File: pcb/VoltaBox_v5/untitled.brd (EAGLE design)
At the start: 80 x 60 mm, 63 parts, among them J1 0, X1 112J-TDAR-R(MICROSD), X2 52892-0895, X3 52892-0895, X4 XT30PW-F, X6 XT60PW-M, X7 KLS1-233

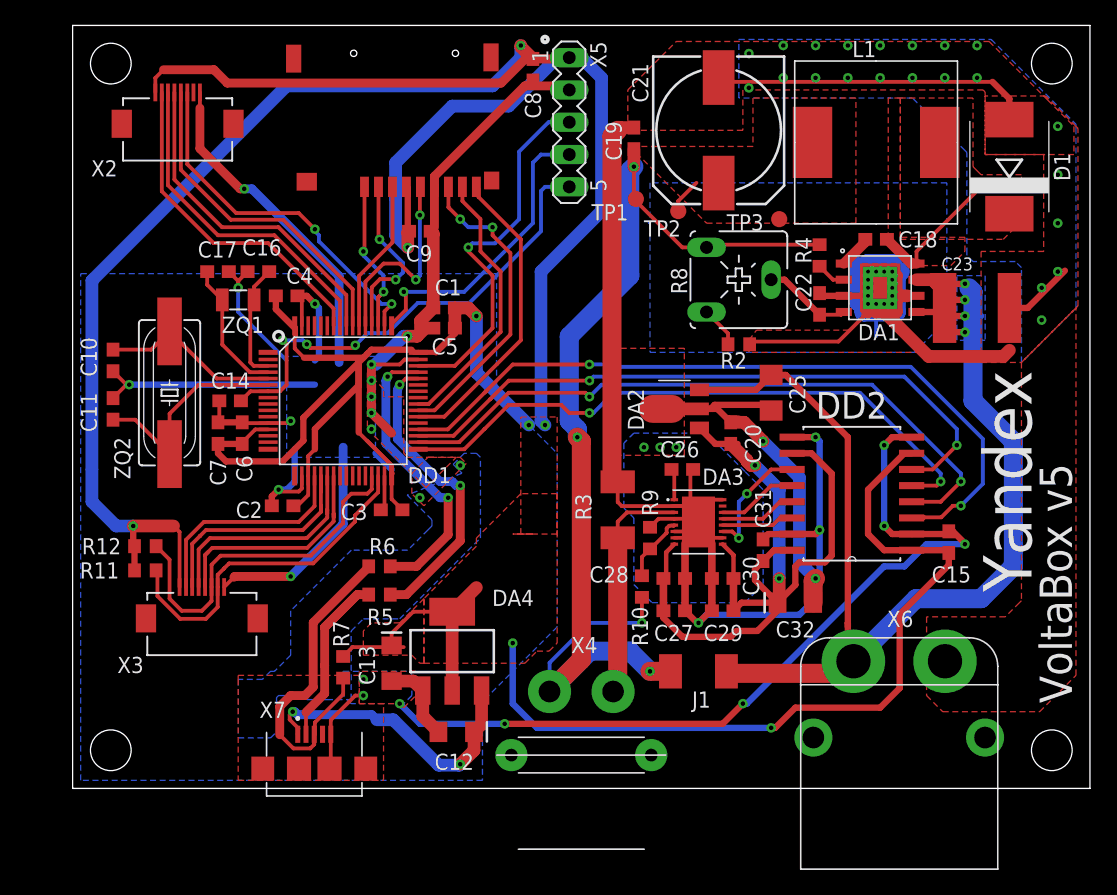
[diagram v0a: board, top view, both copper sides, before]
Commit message: VB5 DC-DC GND fixed, STM32 boot pin connected
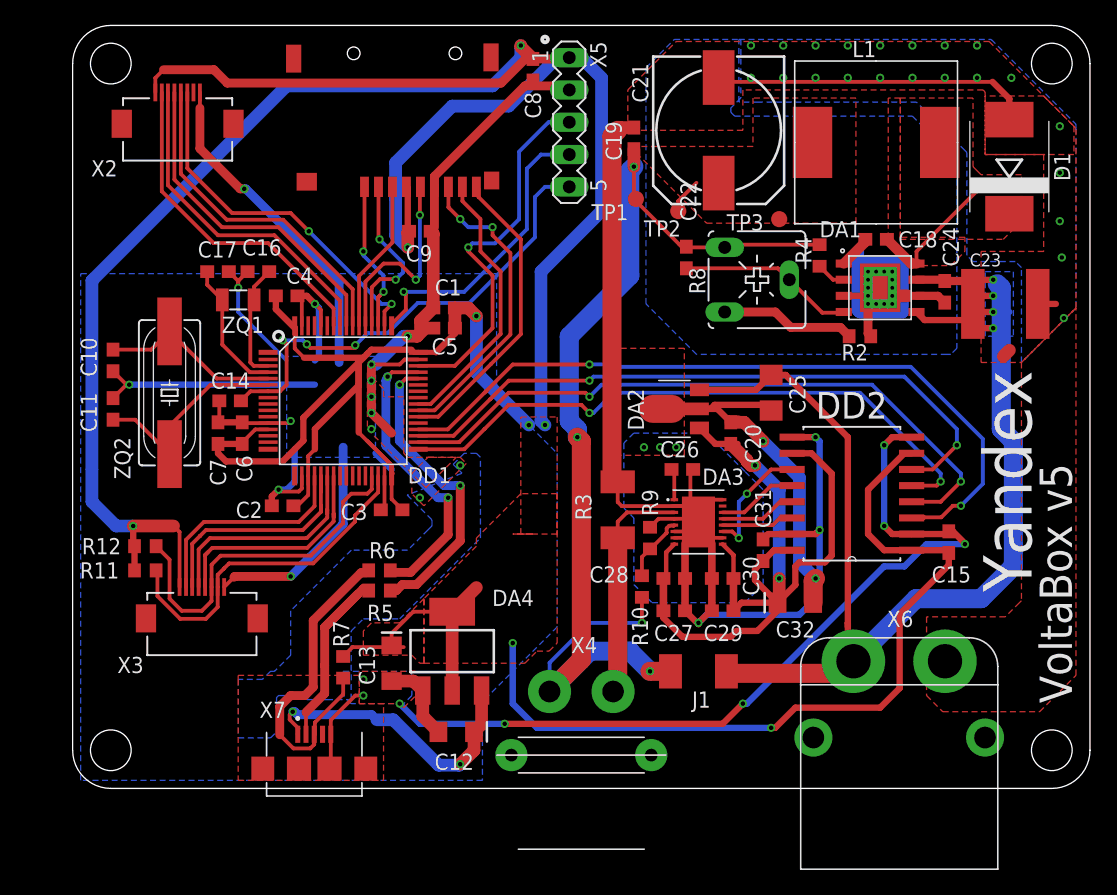
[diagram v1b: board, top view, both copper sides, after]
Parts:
- added C24: 0.1u, eagle-ltspice:C0603
- moved C22 11.1 mm to (48.3, 41.8)
- moved R2 9.55 mm to (61.9, 35.6)
- moved C23 2.25 mm to (73.3, 38.1)
- moved R8 1.43 mm to (53.8, 40.0)
- moved R5 0.32 mm to (24.1, 15.6)
- moved R6 0.32 mm to (24.1, 17.1)
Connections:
- net +12V: now also C24.1
- net +4V: now also C22.2
- net AGND: now also C24.2; no longer C22.2
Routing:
- net AGND: track 213.2 -> 186.3 mm, vias 30 -> 29
- net N$22: track 3.24 -> 10.6 mm
- net N$10: track 6.95 -> 13.9 mm
- net +12V: track 97.0 -> 101.5 mm
- net GND: track 226.2 -> 227.8 mm
- net N$2: track 19.0 -> 18.5 mm
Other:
- outline, holes or cut-outs redrawn

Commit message: additional oled connector added, some small fixes, swd relayout
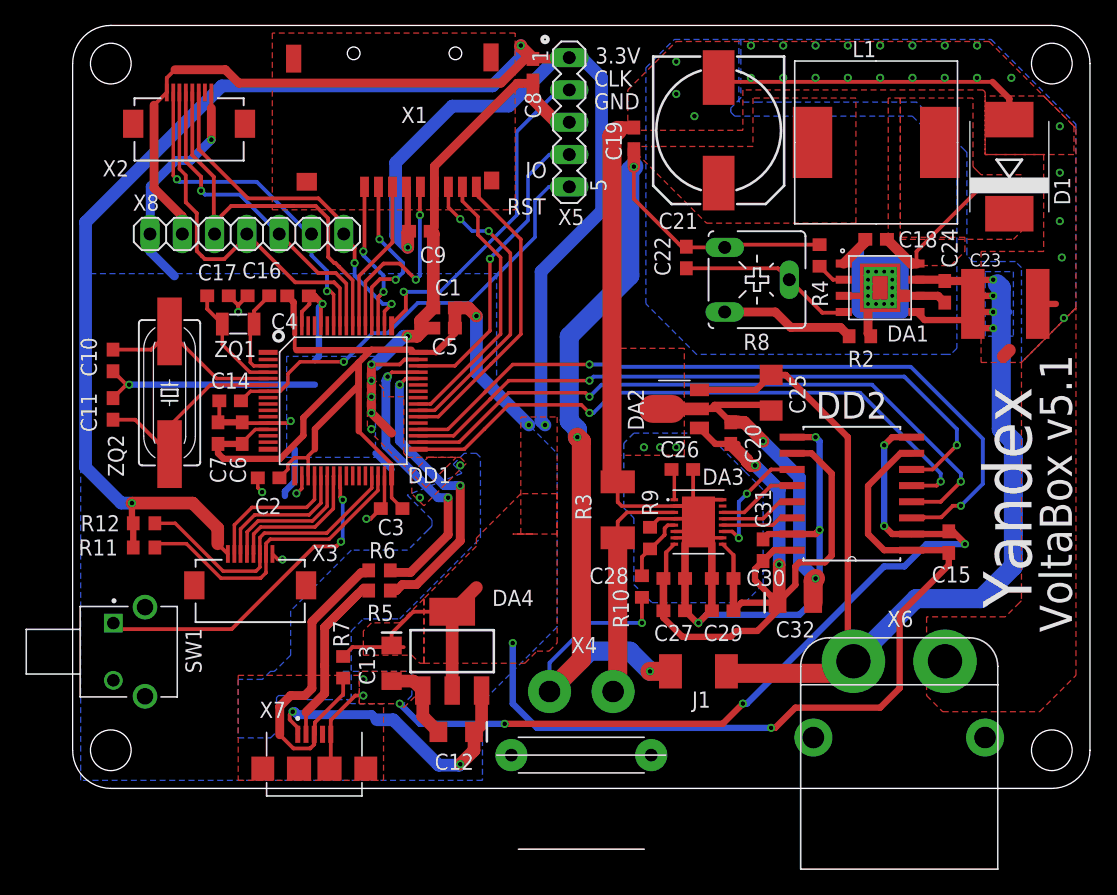
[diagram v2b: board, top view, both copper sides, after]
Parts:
- removed TP1, TP2, TP3: TPSQB1,27, testpad:B1,27
- added SW1: FSMRA6JH, FSMRA6JH:TE_FSMRA6JH
- added X8: (no value), pinhead:1X07
- R2: value 3.3K -> 2.7K
- moved X3 4.60 mm to (14.0, 21.3)
- moved C2 2.46 mm to (15.4, 24.4)
- moved C16 1.90 mm to (14.6, 38.7)
- moved C17 1.90 mm to (11.4, 38.7)
- moved ZQ1 1.90 mm to (13.0, 36.5)
- moved R11 1.80 mm to (5.62, 18.9)
- moved R12 1.80 mm to (5.62, 20.9)
- moved C4 0.90 mm to (17.7, 38.7)
- moved X2 0.90 mm to (9.15, 57.6)
- moved C3 0.10 mm to (25.1, 22.0)
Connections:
- new net N$17: DD1.24, SW1.1
- net +3V3: now also X8.2
- net +4V: no longer TP1.TP, TP2.TP, TP3.TP
- net GND: now also SW1.2, SW1.S1, SW1.S2, X5.3, X8.1; no longer X5.2
- net OLED_CS: now also X8.7
- net OLED_DC: now also X8.6
- net OLED_MOSI: now also X8.4
- net OLED_RS: now also X8.5
- net OLED_SCK: now also X8.3
- net SWCLK: now also X5.2; no longer X5.4
- net SWDIO: now also X5.4; no longer X5.3
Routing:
- net GND: track 227.8 -> 197.8 mm, vias 23 -> 25
- net N$17: track 0.00 -> 26.3 mm, vias 0 -> 2
- net +3V3: track 344.4 -> 355.9 mm
- net OLED_SCK: track 26.6 -> 36.8 mm
- net N$30: track 19.2 -> 11.3 mm
- net AGND: track 186.3 -> 193.4 mm, vias 29 -> 33
- net N$28: track 17.9 -> 11.3 mm
- net N$29: track 17.7 -> 11.3 mm
- net N$31: track 17.3 -> 11.3 mm
- net SWDIO: track 29.3 -> 24.1 mm
- net N$27: track 28.5 -> 23.6 mm
- net OLED_MOSI: track 26.6 -> 30.2 mm
- net N$24: track 27.4 -> 24.1 mm
- net SWCLK: track 23.5 -> 26.7 mm
- net NRESET: track 37.8 -> 34.9 mm, vias 3 -> 1
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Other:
- board text added: "3.3V"
- board text added: "CLK"
- board text added: "GND"
- board text added: "IO"
- board text added: "RST"
- board text added: "VoltaBox v5.1"
- board text added: "X1"
- board text removed: "VoltaBox v5"
